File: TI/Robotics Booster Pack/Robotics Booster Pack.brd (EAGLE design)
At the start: 68.6 x 76.2 mm, 118 parts, among them U1 DRV8800, U10 74LVTH125.RGY, U11 SCHA4B0400, U12 BLUETOOTH-RN41", U13 XBEE-1XBEE-1_LOCK, U14 FDMA3028N, U2 DRV8800, U3 DRV8800, U4 DRV8800, U5 TPS5331[8/9].DQP, U6 TPS62082.DSG, U7 PCA9557.RGV, U8 MPU-6050, U9 INA220.DGS

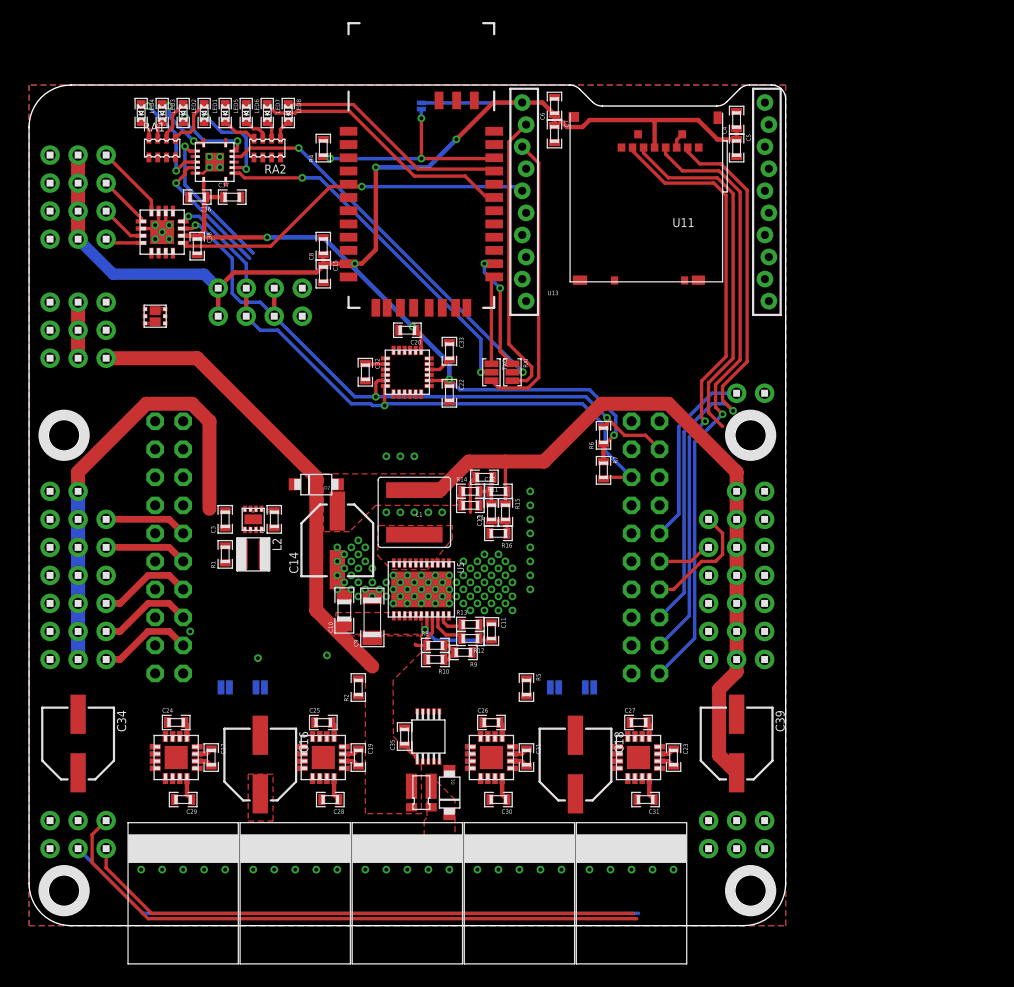
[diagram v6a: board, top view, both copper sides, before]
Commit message: Making progress on PCB re-layout. Moved some pins around to make routing _much_ easier, along with the added improvements.
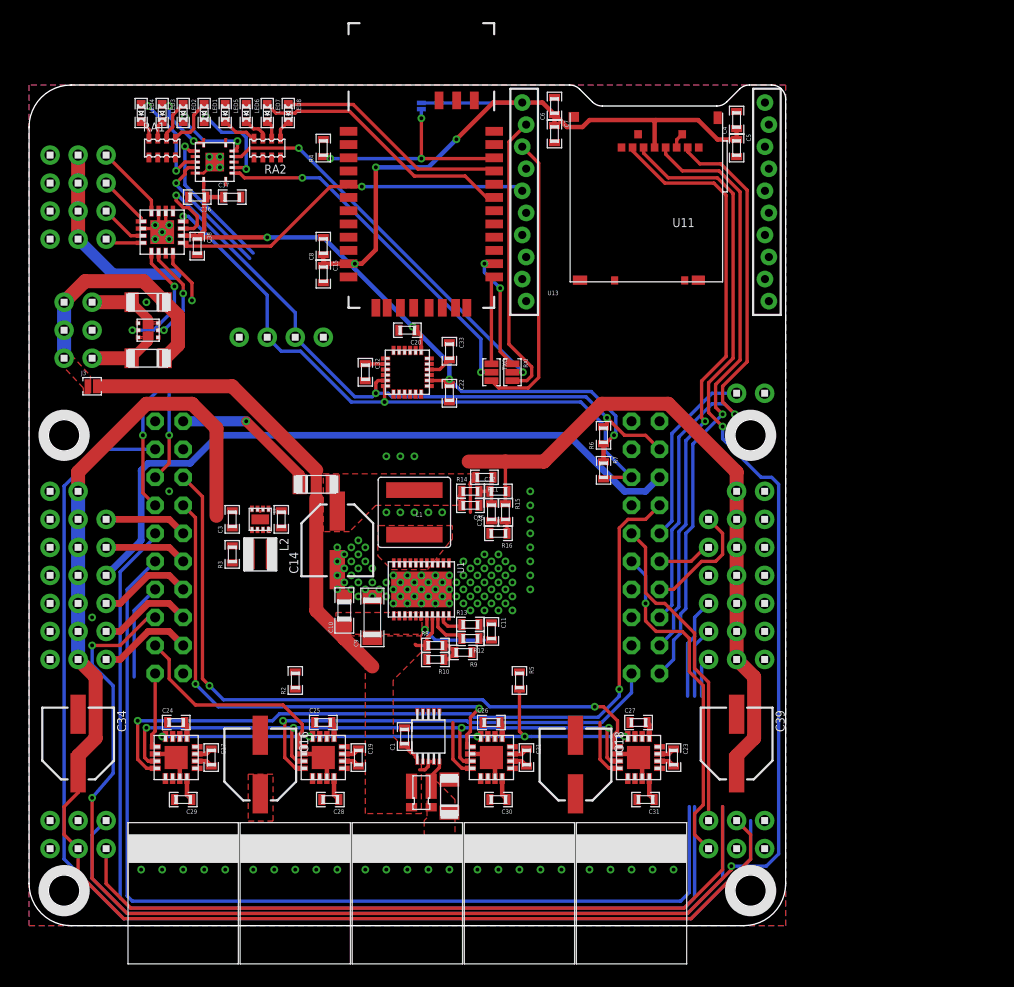
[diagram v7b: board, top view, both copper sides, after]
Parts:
- removed H8: 1X3, headers(.1in):1X3
- removed J5, J6, J7, J8: (no value), solderjumper:2.LRG
- removed U$9: 2X4, headers(.1in):2X4
- removed U14: FDMA3028N, freescale:MICROFET.2X2
- added D3, D4: CDBMT2100-HF, comchip:SOD-123H
- added J3: (no value), solderjumper:2.LRG
- added Q1: (no value), fairchild:MICROFET.2X2
- added U$6: 1X4, headers(.1in):1X4
- D1, D2: value (none) -> CDBMT2100-HF; device nxp:SOD123W -> comchip:SOD-123H
- R1: value 178k -> 1u; device standardparts:0603 -> vishay:0612
- R3: value 1u -> 178k; device vishay:0612 -> standardparts:0603
- U1: value DRV8800 -> TPS5331[8/9].DQP; device packages(ti):RTY.16 -> packages(ti):DQP.22
- U2: value DRV8800 -> TPS62082.DSG; device packages(ti):RTY.16 -> packages(ti):DSG
- U5: value TPS5331[8/9].DQP -> DRV8800; device packages(ti):DQP.22 -> packages(ti):RTY.16
- U6: value TPS62082.DSG -> DRV8800; device packages(ti):DSG -> packages(ti):RTY.16
- moved R1 28.0 mm to (35.6, 12.1), turned to 270 degrees
- moved R3 27.6 mm to (18.4, 33.7), turned to 90 degrees
- moved U1 26.9 mm to (35.6, 30.5), turned to 180 degrees
- moved U5 26.9 mm to (13.3, 15.2), turned to 0 degrees
- moved U6 22.5 mm to (26.7, 15.2), turned to 0 degrees
- moved U2 22.3 mm to (21.0, 36.8), turned to 270 degrees
- moved C1 21.8 mm to (34.0, 17.1), turned to 90 degrees
- moved C35 21.8 mm to (40.0, 38.1), turned to 180 degrees
- moved R2 5.75 mm to (24.1, 22.2)
- moved H14 5.68 mm to (66.7, 9.53), turned to 180 degrees
- moved H9 1.27 mm to (5.71, 56.5)
- moved H7 1.27 mm to (3.17, 56.5)
- moved R5 0.90 mm to (44.5, 22.2)
- moved C2 0.63 mm to (22.9, 36.8)
- moved C3 0.63 mm to (18.4, 36.8)
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- renumbered H21 to J1
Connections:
- removed net N$16: H8.1, H8.2, H8.3
- removed net VIN: C2.1, D2.P$2, U$8.VBUS, U6.8
- new net VFET: D3.1, D4.1, H7.1, H7.2, H7.3, J3.1
- new net VSERVO: C12.2, C14.+, C39.+, D2.2, H2.1, H2.2, H2.3, H2.4, H2.5, H2.6, H22.1, L1.2, R15.1
- net 3.3V: now also C1.1, R3.2, U$6.1, U2.5; no longer C35.1, R1.2, U$9.1, U$9.2, U6.5
- net 3.3V.PG: now also R3.1, U2.6; no longer R1.1, U6.6
- net 5.0V: now also C2.1, D2.1, U$8.VBUS, U2.8; no longer C12.2, C14.+, C39.+, D2.P$1, H2.1, H2.2, H2.3, H2.4, H2.5, H2.6, H22.1, L1.2, R15.1
- net 5V.PG: now also U1.3, U2.1; no longer U5.3, U6.1
- net FET0.D: now also D3.2, Q1.6, Q1.PAD@1; no longer U14.6, U14.PAD@1
- net FET0.G: now also Q1.2; no longer U14.2
- net FET1.D: now also D4.2, H9.3, Q1.3, Q1.PAD@2; no longer H9.2, U14.3, U14.PAD@2
- net FET1.G: now also Q1.5; no longer U14.5
- net GND: now also C1.2, D1.2, H9.2, Q1.1, Q1.4, U$6.4, U2.3, U5.12, U5.2, U5.7, U6.12, U6.7; no longer C35.2, D1.P$1, H7.1, H7.2, H7.3, U$9.7, U$9.8, U1.12, U1.2, U1.7, U14.1, U14.4, U2.12, U2.7, U6.3
- net I2C.SCL: now also U$6.3; no longer U$9.5, U$9.6
- net I2C.SDA: now also U$6.2; no longer U$9.3, U$9.4
- net M.EN: now also U5.3, U6.3; no longer U1.3, U2.3
- net M.MODE: now also U5.16, U6.16; no longer U1.16, U2.16
- net M0+: now also U5.6; no longer U1.6
- net M0-: now also U5.9; no longer U1.9
- net M0.DIR: now also U$8.PF0, U5.4; no longer J6.1, U$8.PC4, U1.4
- net M0.SPD: now also U$8.PA7, U5.1; no longer J5.1, U$8.PD0, U1.1
- net M1+: now also U6.6; no longer U2.6
- net M1-: now also U6.9; no longer U2.9
- net M1.DIR: now also U$8.PF4, U6.4; no longer J6.2, U$8.PC7, U2.4
- net M1.SPD: now also U$8.PA6, U6.1; no longer J5.2, U$8.PD1, U2.1
- net M2.DIR: now also U$8.PC4; no longer J8.1, U$8.PF0
- net M2.SPD: now also U$8.PD1; no longer J7.1, U$8.PA6
- net M3.DIR: now also U$8.PC7; no longer J8.2, U$8.PF4
- net M3.SPD: now also U$8.PD0; no longer J7.2, U$8.PA7
- net N$10: now also U1.1; no longer U5.1
- net N$12: now also U2.7; no longer U6.7
- net N$13: now also U5.11; no longer U1.11
- net N$15: now also C35.2, U1.10, U1.11, U1.6, U1.7, U1.8, U1.9; no longer C1.2, U5.10, U5.11, U5.6, U5.7, U5.8, U5.9
- net N$18: now also U5.13; no longer U1.13
- net N$19: now also U6.13; no longer U2.13
- net N$2: now also C35.1, U1.4; no longer C1.1, U5.4
- net N$22: now also D1.1, R1.1@1, R1.1@2; no longer D1.P$2, R3.1@1, R3.1@2
- net N$25: now also U6.11; no longer U2.11
- net N$3: now also U1.20; no longer U5.20
- net N$38: now also U5.10; no longer U1.10
- net N$39: now also U6.10; no longer U2.10
- net N$4: now also U1.18; no longer U5.18
- net N$5: now also U1.21; no longer U5.21
- net N$8: now also U1.2; no longer U5.2
- net VBAT: now also J3.2, R1.2@1, R1.2@2, U1.12, U1.13, U1.14, U1.15, U1.16, U1.17, U1.19, U5.8, U6.8; no longer H9.3, R3.2@1, R3.2@2, U1.8, U2.8, U5.12, U5.13, U5.14, U5.15, U5.16, U5.17, U5.19
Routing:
- net SPI.MOSI: track 32.7 -> 169.4 mm, vias 0 -> 4
- net SVRO3: track 0.00 -> 122.8 mm
- net SVRO4: track 0.00 -> 101.8 mm
- net SVRO5: track 0.00 -> 94.2 mm
- net M0.DIR: track 0.00 -> 70.0 mm, vias 0 -> 2
- net M.EN: track 0.00 -> 62.2 mm, vias 0 -> 5
- net AD3: track 0.00 -> 61.8 mm
- net VSERVO: track 0.00 -> 61.3 mm
- net M3.SPD: track 0.10 -> 60.8 mm, vias 0 -> 2
- net 5.0V: track 67.5 -> 13.4 mm, vias 0 -> 1
- net M.MODE: track 0.00 -> 47.6 mm, vias 0 -> 5
- net M2.SPD: track 0.00 -> 47.4 mm, vias 0 -> 2
- net M1.DIR: track 0.00 -> 39.9 mm, vias 0 -> 1
- net QEI1.B: track 0.00 -> 31.0 mm, vias 0 -> 1
- net QEI1.A: track 0.00 -> 29.4 mm
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- added copper zone on layer 1, net VFET
- added copper zone on layer 1, net VSERVO
- removed copper zone on layer 1, net 5.0V
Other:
- board text added: "VFET"
- board text removed: "1 || 2"
- board text removed: "VIN"

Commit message: Replaced 5v regulator circuit with TPS5450 Added more power options in the form of SMD Jumpers Added IO Expander-controlled Servo FET Swapped positions of XBee and extra IO/FETs to make routing simpler Connected 5v and 3.3v from BoosterPack to Launchpad Added header to connect to UART0 (Wireless programming/debugging)
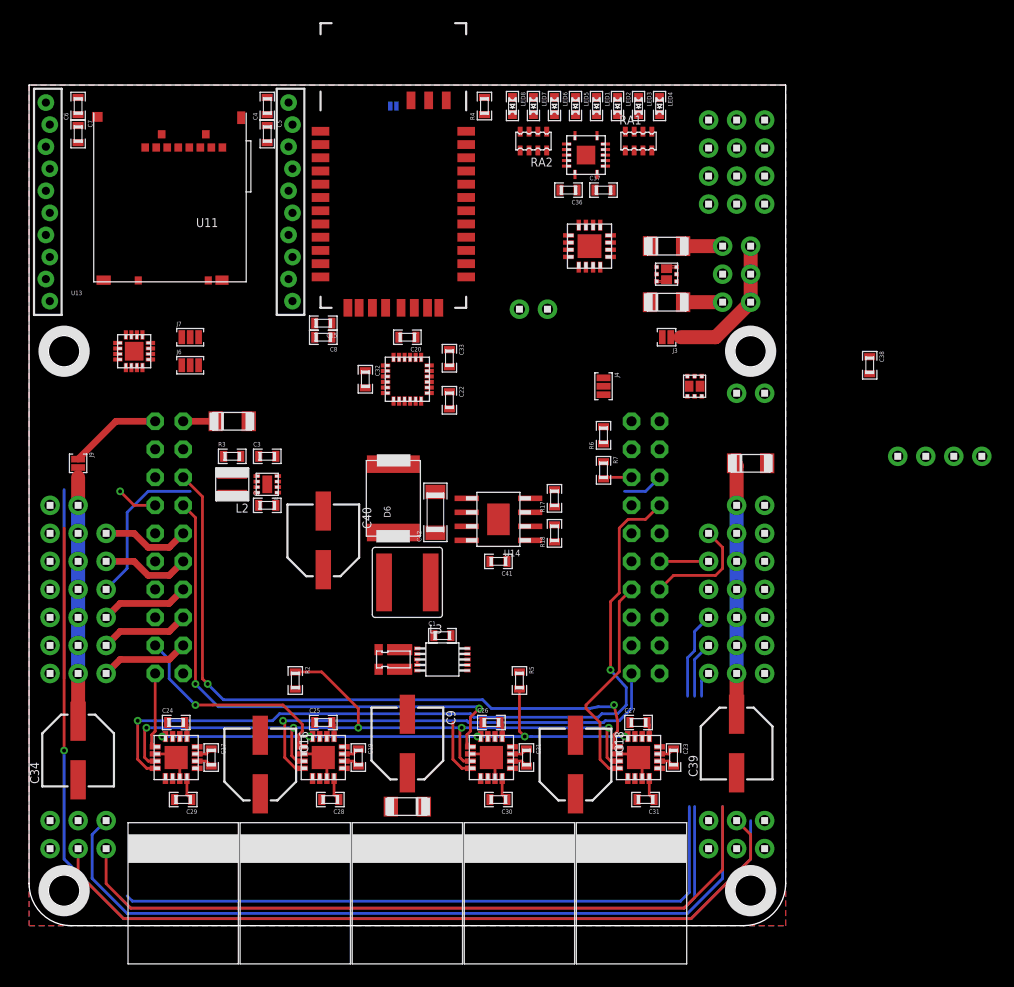
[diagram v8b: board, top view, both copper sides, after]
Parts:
- removed C10: 4.7uF, standardparts:0805
- removed C11: 1uF, standardparts:0603
- removed C12, C35: .1uF, standardparts:0603
- removed C13: 1nF, standardparts:0603
- removed C14: 100uF, microbuilder:PANASONIC_D
- removed H22, H26: 1X2, headers(.1in):1X2
- removed L1: 2.2uH, coilcraft:XAL6030
- removed R10: 1k, standardparts:0603
- removed R11, R12: 100k, standardparts:0603
- removed R13: 191k, standardparts:0603
- removed R14: 2.55k, standardparts:0603
- removed R15: 76.8k, standardparts:0603
- removed R16: 10k, standardparts:0603
- removed R8: 200k, standardparts:0603
- removed R9: 86.6k, standardparts:0603
- removed RXI, TXO: (no value), solderjumper:3.LRG.12
- added C40: 330uF, microbuilder:PANASONIC_D
- added C41: 10nF, standardparts:0603
- added C42: 10uF, standardparts:1206
- added D5: CDBMT2100-HF, comchip:SOD-123H
- added D6: CDBC5XXX-G, comchip:DO-214AB
- added J4: (no value), solderjumper:3.LRG.12
- added J6, J7: (no value), solderjumper:3.LRG
- added J9: (no value), solderjumper:2.LRG.PASTE
- added L3: INDUCTOR.XAL6060, coilcraft:XAL6060
- added Q2: (no value), fairchild:MICROFET.2X2
- added R17: 10k, standardparts:0603
- added R18: 2.87k, standardparts:0603
- added U$15: 1X2, headers(.1in):1X2
- added U14: TPS54X0, packages(ti):DDA
- C39: value 100uF -> 220uF
- C9: value 22uF -> 100uF; device standardparts:1206 -> microbuilder:PANASONIC_D
- H1, H2, H4, H5: value 1X6 -> 1X7; device headers(.1in):1X6 -> headers(.1in):1X7
- U1: value TPS5331[8/9].DQP -> TS3A44159.RGT; device packages(ti):DQP.22 -> packages(ti):RGT.16
- moved H10 64.8 mm to (66.7, 73.0)
- moved H7 62.2 mm to (65.4, 56.5), turned to 90 degrees
- moved C38 61.9 mm to (76.2, 50.8)
- moved U$6 60.7 mm to (78.7, 42.5)
- moved H11 59.8 mm to (64.1, 73.0)
- moved H9 57.4 mm to (62.9, 61.6)
- moved H12 54.7 mm to (61.6, 73.0)
- moved J3 52.3 mm to (57.8, 53.3), turned to 180 degrees
- moved D3 47.3 mm to (57.8, 61.6), turned to 0 degrees
- moved D4 47.3 mm to (57.8, 56.5), turned to 0 degrees
- moved Q1 47.3 mm to (57.8, 59.1)
- moved LED4 47.0 mm to (57.1, 74.3)
- moved LED3 43.2 mm to (55.2, 74.3)
- moved RA1 43.2 mm to (55.2, 71.1)
- moved U11 43.2 mm to (19.7, 73.7)
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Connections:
- removed net N$23: LED3.P$2, RA1.4
- removed net N$30: LED1.P$1, RA1.8
- removed net N$31: LED2.P$1, RA1.6
- removed net N$46: LED7.P$2, RA2.3
- removed net N$47: LED6.P$2, RA2.5
- removed net N$48: LED5.P$2, RA2.7
- removed net UART.RXI: RXI.2, U$8.PB0, U10.5
- removed net UART.TXO: TXO.2, U$8.PB1, U10.2
- new net N$16: J4.2, Q2.3, Q2.6, Q2.PAD@1, Q2.PAD@2
- new net N$33: C41.1, U14.1
- new net N$34: C41.2, D6.1, L3.1, U14.8
- new net N$35: R17.1, R18.2, U14.4
- new net SRVO.EN: Q2.2, Q2.5, U7.12
- new net UART0.RXI: U1.4
- new net UART0.TXO: U1.16
- new net UART1.RXI: U$8.PB0, U1.8, U10.5
- new net UART1.TXO: U$8.PB1, U1.10, U10.2
- net 3.3V: now also J6.1, J7.1, J9.1, U$8.3.3V, U1.14; no longer C34.+, H26.1, H5.1, H5.2, H5.3, H5.4, H5.5, H5.6
- net 5.0V: now also C40.+, D2.2, J4.3, L3.2, R17.2; no longer D2.1, U$8.VBUS
- net 5V.PG: no longer R11.2, U1.3
- net AD0: now also H6.1, U$8.PD2; no longer H6.6, U$8.PE3
- net AD1: now also H6.2, U$8.PD3; no longer H6.5, U$8.PE2
- net AD2: now also H6.3, U$8.PE0; no longer H6.4, U$8.PE1
- net AD3: now also H6.4, U$8.PE1; no longer H6.3, U$8.PE0
- net AD4: now also H6.5, U$8.PE2; no longer H6.2, U$8.PD3
- net AD5: now also H6.6, U$8.PE3; no longer H6.1, U$8.PD2
- net BT.RXI: now also U1.13, U1.5; no longer RXI.1
- net BT.TXO: now also U1.1, U1.9; no longer TXO.1
- net FET0.G: now also U7.4; no longer U7.9
- net FET1.G: now also U7.5; no longer U7.10
- net GND: now also C40.-, C42.2, D5.2, D6.2, H1.7, H4.7, J6.3, J7.3, R18.1, U1.6, U14.6, U14.PAD; no longer C10.2, C11.1, C14.-, C9.2, H22.2, H26.2, R12.1, R13.2, R16.2, R9.1
- net IO0: now also U7.10; no longer U7.4
- net IO1: now also U7.9; no longer U7.5
- net IO2: now also U7.8; no longer U7.7
- net IO3: now also U7.7; no longer U7.8
- net M.EN: now also U7.11; no longer U7.12
- net N$1: now also D2.1, U$8.VBUS; no longer U$8.3.3V
- net N$10: now also LED2.P$1, RA1.4; no longer C13.1, R15.2, R16.1, U1.1
- net N$11: now also LED1.P$1, RA1.2; no longer R10.1, R8.2, R9.2
- net N$14: now also LED8.P$2, RA2.7; no longer C12.1, C13.2, R14.2
- net N$15: now also LED6.P$2, RA2.3; no longer C35.2, L1.1, R14.1, U1.10, U1.11, U1.6, U1.7, U1.8, U1.9
- net N$17: now also LED5.P$2, RA2.1; no longer LED4.P$2, RA1.2
- net N$2: now also J6.2, U1.2; no longer C35.1, U1.4
- net N$22: now also C9.+
- net N$3: now also J7.2, U1.12; no longer R12.2, U1.20
- net N$4: now also C34.+, H5.1, H5.2, H5.3, H5.4, H5.5, H5.6, H5.7, J9.2; no longer C11.2, R11.1, U1.18
- net N$5: now also LED4.P$2, RA1.8; no longer R13.1, U1.21
- net N$8: now also LED3.P$2, RA1.6; no longer R10.2, U1.2
- net N$9: now also LED7.P$2, RA2.5; no longer LED8.P$2, RA2.1
- net VBAT: now also C42.1, J4.1, U14.7; no longer C10.1, C9.1, R8.1, U1.12, U1.13, U1.14, U1.15, U1.16, U1.17, U1.19
- net VSERVO: now also D5.1, H2.7, Q2.1, Q2.4; no longer C12.2, C14.+, D2.2, H22.1, L1.2, R15.1
- net XBEE.RXI: now also U1.11, U1.3; no longer RXI.3
- net XBEE.TXO: now also U1.15, U1.7; no longer TXO.3
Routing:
- net 3.3V: track 280.1 -> 79.6 mm, vias 7 -> 0
- net SPI.MOSI: track 169.4 -> 0.00 mm, vias 4 -> 0
- net I2C.SCL: track 62.9 -> 0.00 mm, vias 3 -> 0
- net SPI.SCLK: track 56.0 -> 0.00 mm, vias 1 -> 0
- net I2C.SDA: track 58.5 -> 2.60 mm, vias 2 -> 0
- net SPI.!CS: track 54.0 -> 0.00 mm, vias 1 -> 0
- net AD3: track 61.8 -> 8.04 mm
- net SPI.MISO: track 52.7 -> 0.00 mm, vias 1 -> 0
- net !RST: track 50.3 -> 0.00 mm, vias 1 -> 0
- net VBAT: track 58.8 -> 8.86 mm
- net UART.TXO: track 44.3 -> 0.00 mm, vias 3 -> 0
- net UART.RXI: track 44.0 -> 0.00 mm, vias 3 -> 0
- net VSERVO: track 61.3 -> 22.8 mm
- net SVRO4: track 101.8 -> 66.2 mm
- net SVRO5: track 94.2 -> 61.6 mm
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- removed copper zone on layer 1, net N$15
- removed copper zone on layer 1, net N$22
- removed copper zone on layer 1, net VBAT
- removed copper zone on layer 1, net VFET
- removed copper zone on layer 1, net VSERVO
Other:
- outline, holes or cut-outs redrawn
- board text added: "BT"
- board text added: "UART0"
- board text added: "UART1"
- board text removed: "Bluetooth"
